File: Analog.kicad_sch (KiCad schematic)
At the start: 70 parts, among them J1 InL, J2 InR, J3 OutR, J4 OutL, J9 ByPass, K1 G6K-2F-Y, U1 OPA1612, U2 OPA1644, U3 PCM3060, U4 NE5532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

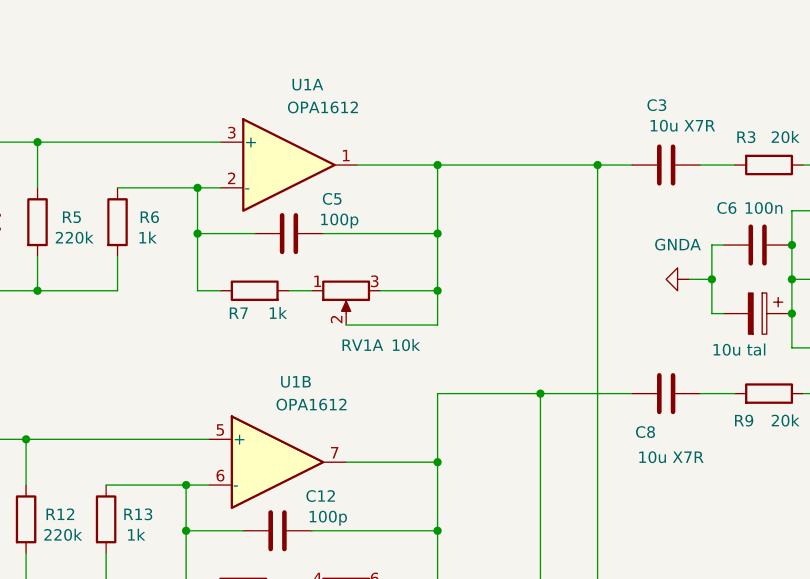
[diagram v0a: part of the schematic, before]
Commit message: Fix typo OPA1612 -> OPA1642. Note: an OPA with FET inputs is necessary here.
/!\  An OPA with FET inputs is necessary here.
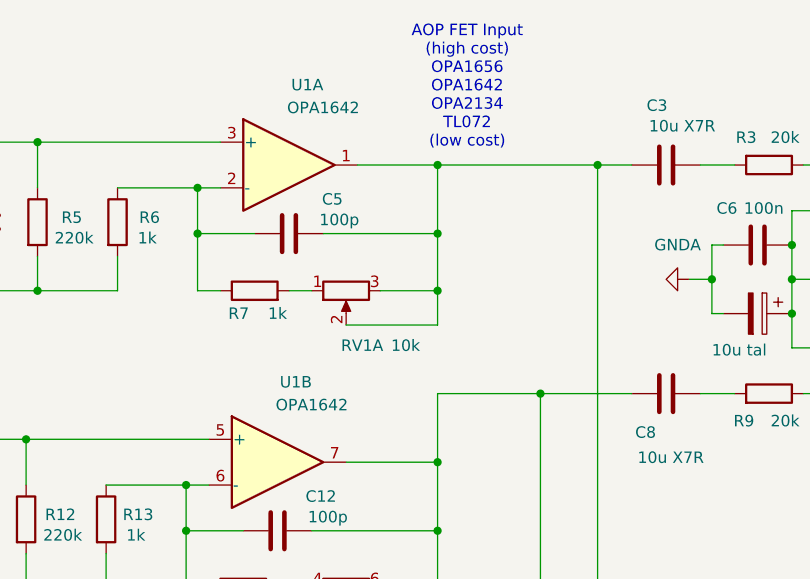
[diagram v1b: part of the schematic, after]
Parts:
- U1: value OPA1612 -> OPA1642
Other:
- note added: "AOP FET Input (high cost) OPA1656 OPA1642 OPA2134 TL072 (low cost)"
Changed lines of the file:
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@@
 		(company "DAD Design")
 	)
+	(text "AOP FET Input\n(high cost)\nOPA1656\nOPA1642\nOPA2134\nTL072\n(low cost)"
+		(exclude_from_sim no)
+		(at 154.432 23.114 0)
+		(effects
+			(font
+				(size 1.27 1.27)
+			)
+		)
+	)
 	(junction
 		(at 181.61 44.45)
@@
 			)
 		)
-		(property "Value" "OPA1612"
+		(property "Value" "OPA1642"
 			(at 137.16 58.42 0)
 			(effects
@@
 			)
 		)
-		(property "Value" "OPA1612"
+		(property "Value" "OPA1642"
 			(at 138.43 25.4 0)
 			(effects

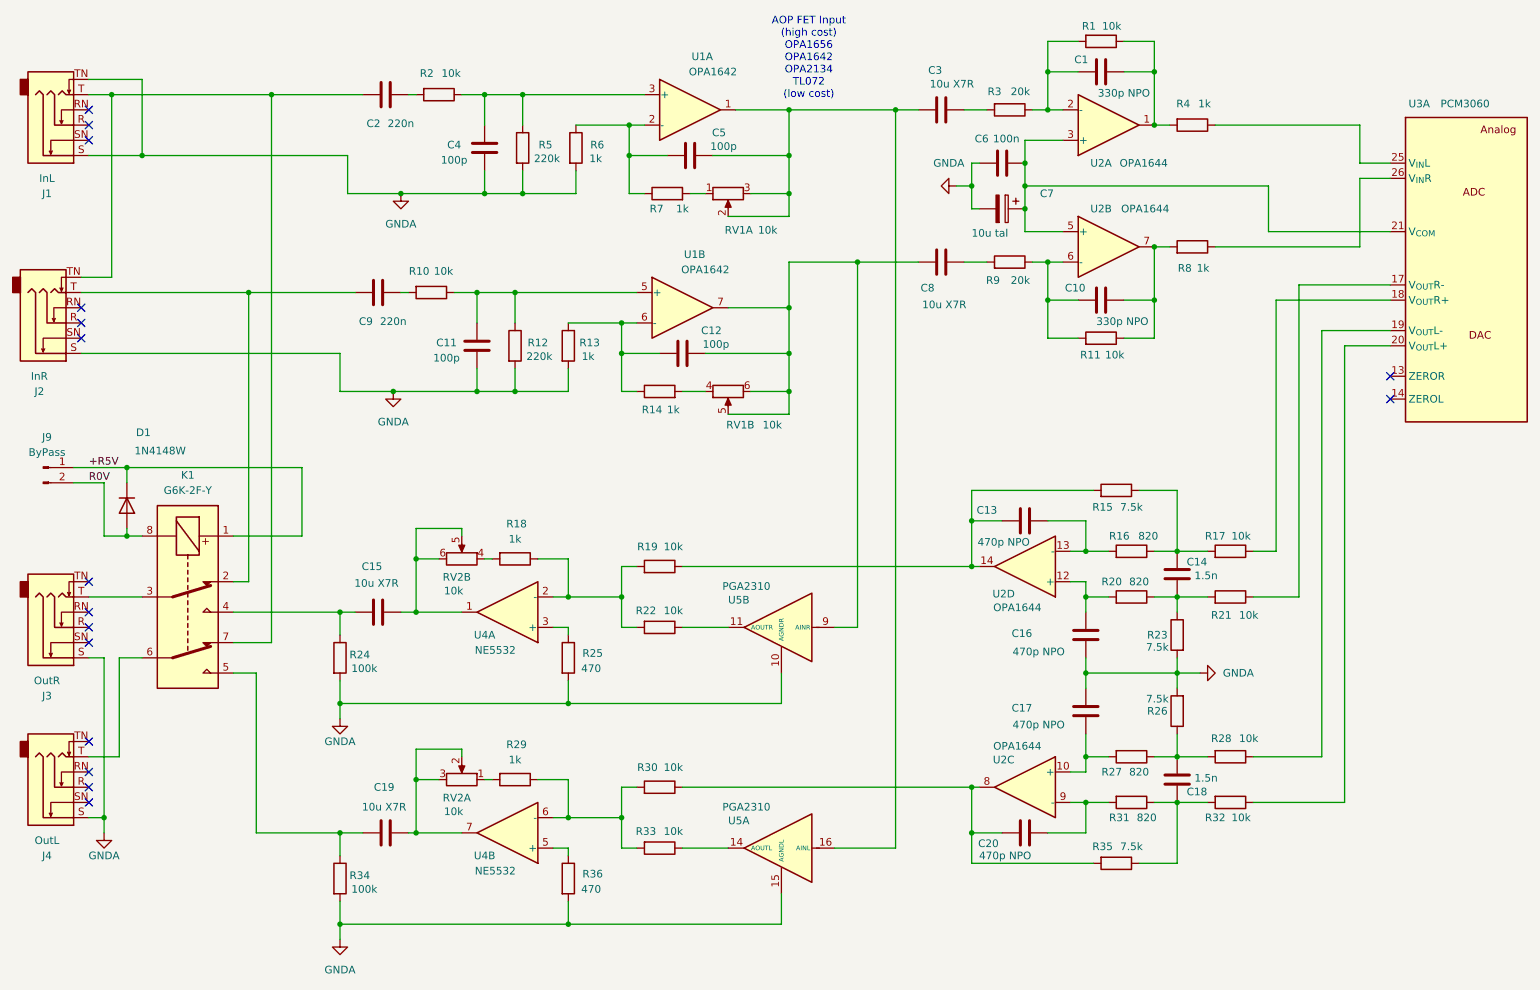
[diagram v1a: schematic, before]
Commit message: Invert output summing stage to maintain correct phase
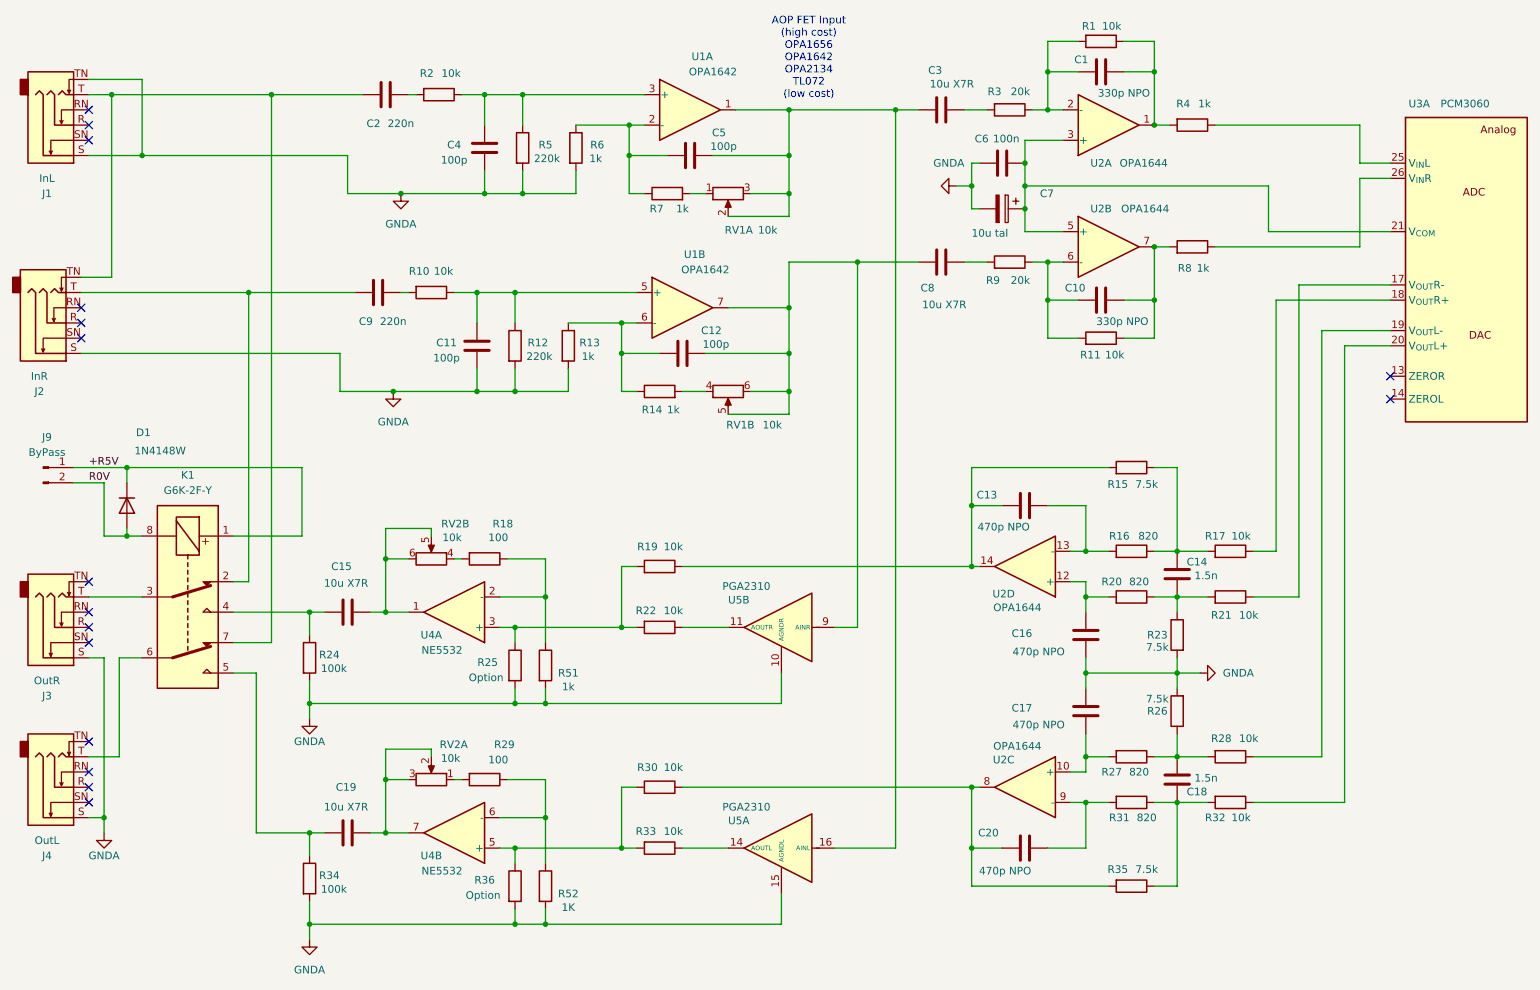
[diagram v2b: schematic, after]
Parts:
- added R51: 1k, Resistor_SMD:R_1206_3216Metric_Pad1.30x1.75mm_HandSolder, symbol Device:R
- added R52: 1K, Resistor_SMD:R_1206_3216Metric_Pad1.30x1.75mm_HandSolder, symbol Device:R
- R18, R29: value 1k -> 100
- R25, R36: value 470 -> Option
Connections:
- net GNDA: now also R51.2, R52.2
- net at R30.2, R33.2: now also R36.1, U4.5 (+); no longer R29.1, U4.6 (-)
- net at R18.1, U4.2 (-): now also R51.1; no longer R19.2, R22.2
- net at R25.1, U4.3 (+): now also R19.2, R22.2
- new net: R29.1, R52.1, U4.6 (-)
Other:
- title: OSCAR Audio 1.0 -> OSCAR Audio 01 V2
- moved on the sheet: C13, C15, C19, C20, R15, R18, R24, R25, R29, R34, R35, R36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

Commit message: Define R25 and R36 to 1k
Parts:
- R25: value Option -> 1K
- R36: value Option -> 1k
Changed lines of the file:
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@@
 			)
 		)
-		(property "Value" "Option"
+		(property "Value" "1k"
 			(at 100.076 162.814 0)
 			(effects
@@
 			)
 		)
-		(property "Value" "Option"
+		(property "Value" "1K"
 			(at 100.584 126.492 0)
 			(effects
